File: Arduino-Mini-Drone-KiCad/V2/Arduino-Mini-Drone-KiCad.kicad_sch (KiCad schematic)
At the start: 76 parts, among them J1 NRF24, J10 BT, J11 PPM, J12 PWR, J13 Open, J2 UART, J3 Motor1, J4 Motor2, J5 Motor3, J6 Motor4, J7 CapHole, J8 MPU9250 + BMP280, J9 SPI Pads, Q1 AO3400A, Q2 AO3400A, Q3 AO3400A, Q4 AO3400A, Q5 AO3401A, SW1 Reset, SW2 Switch, U1 ATmega328P-A, U2 MIC5205YM5, U3 LP5907MFX-3.3, Y1 Crystal_GND2

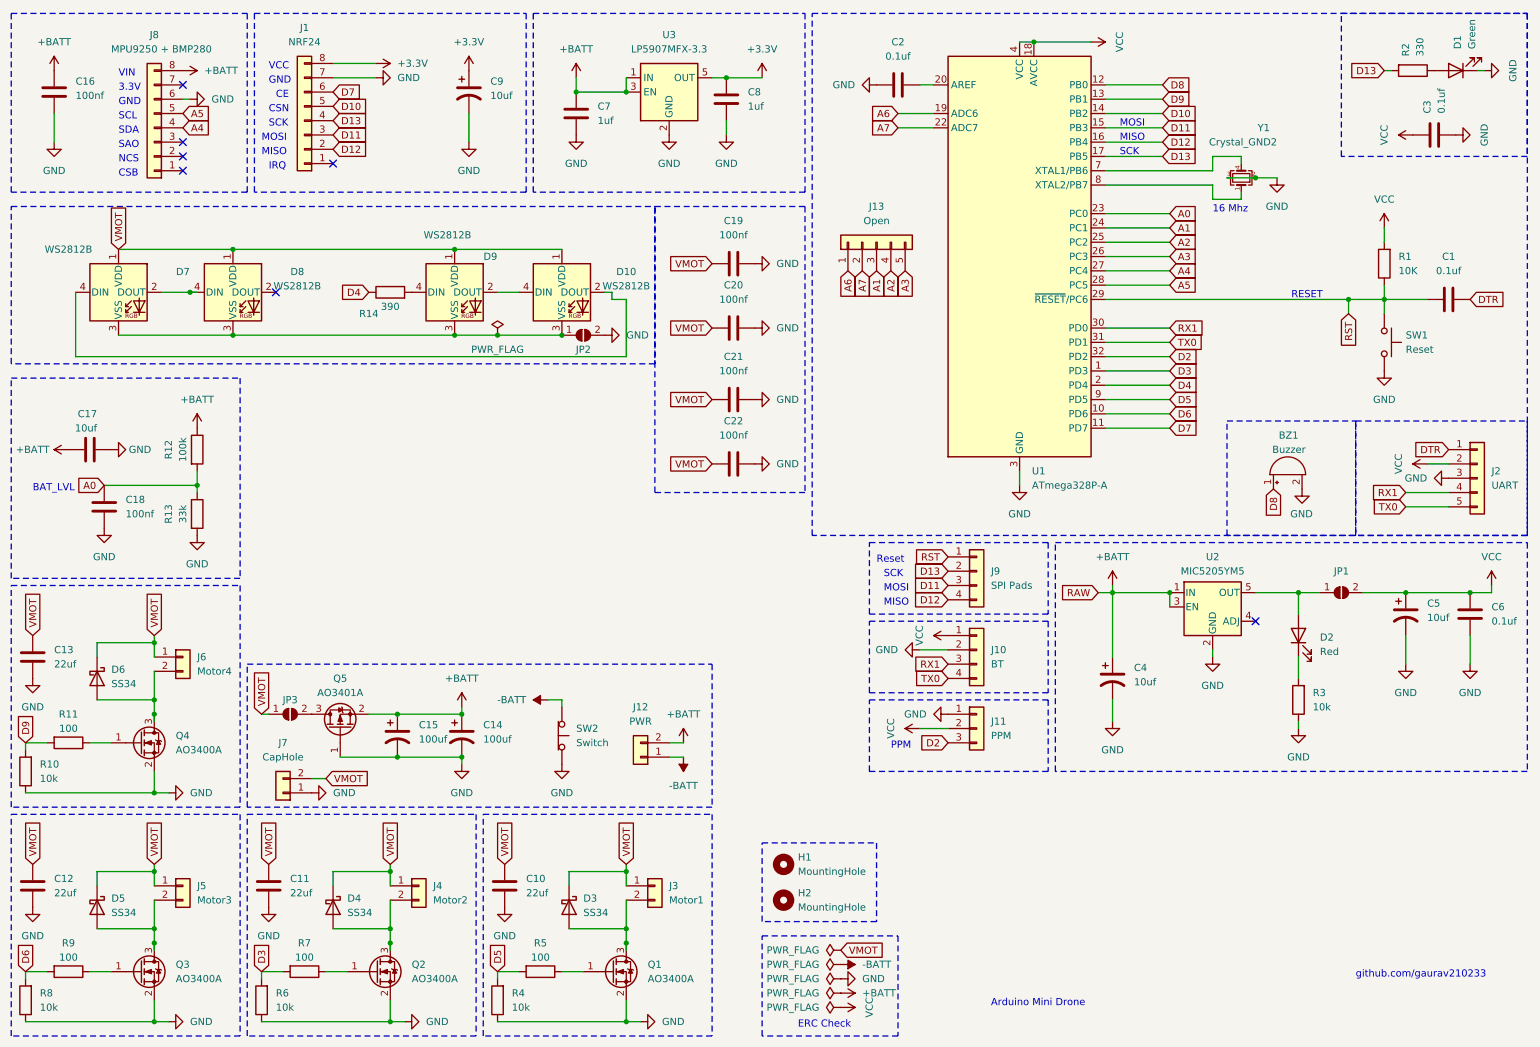
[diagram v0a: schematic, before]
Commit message: Completed Panelized PCB in V2 delete Row 2 PCB for error resolution
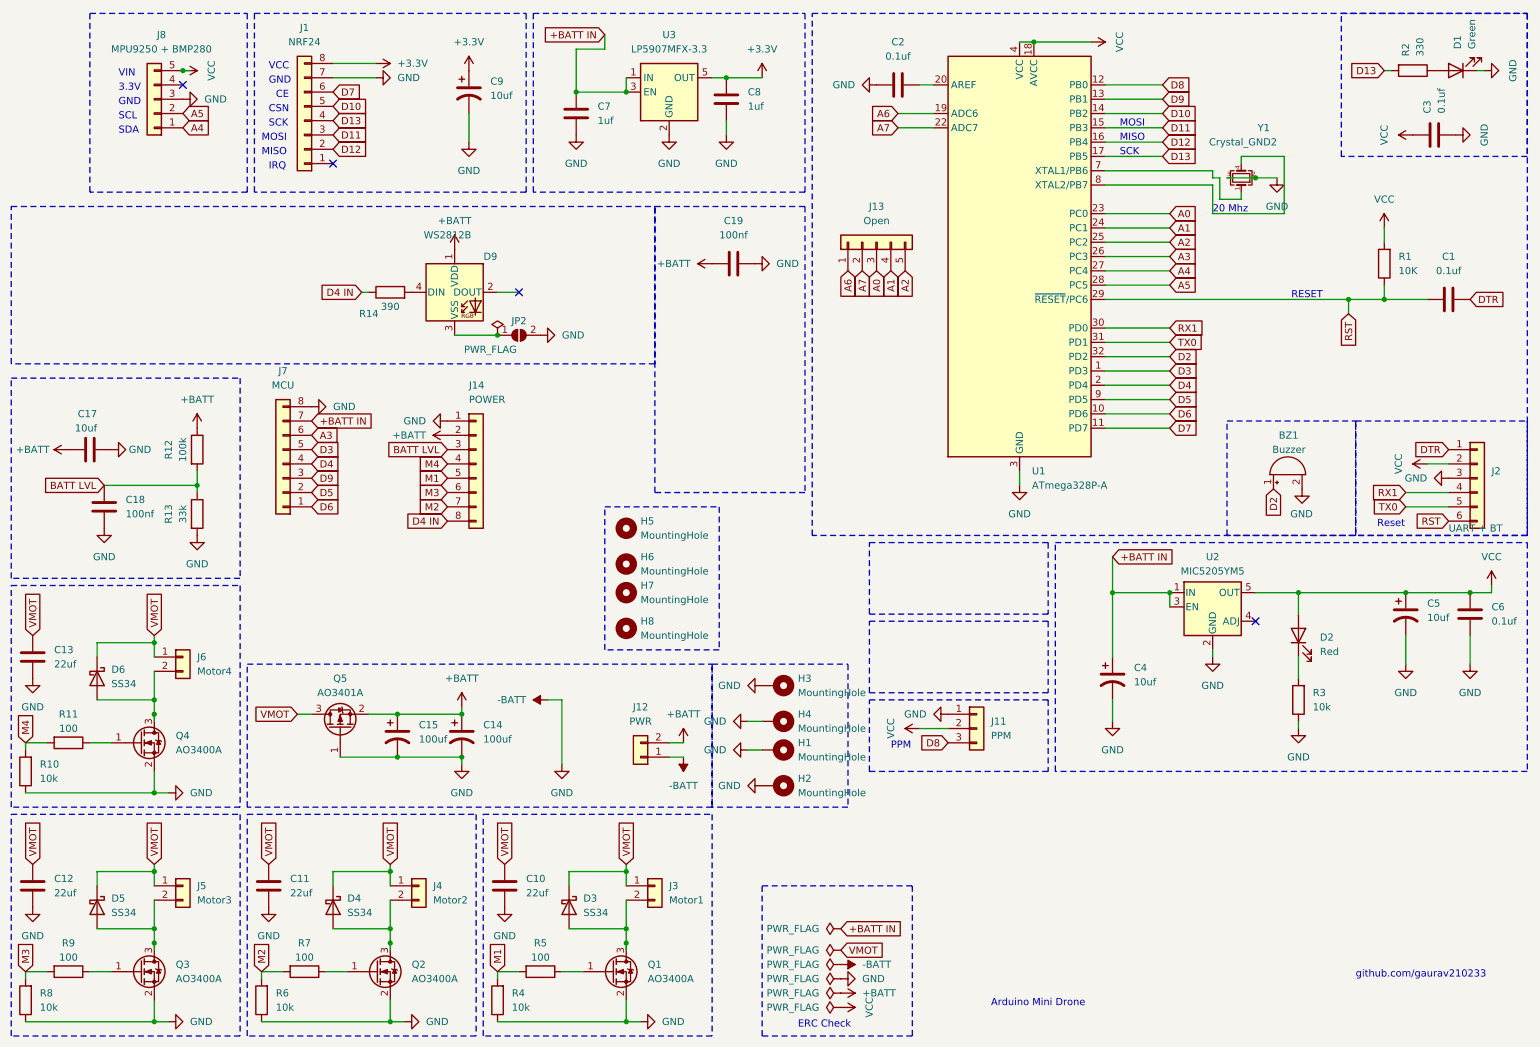
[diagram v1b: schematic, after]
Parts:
- removed C16, C20, C21, C22: 100nf, Capacitor_SMD:C_0603_1608Metric, symbol Device:C
- removed D10, D7, D8: WS2812B, LED_SMD:LED_WS2812B_PLCC4_5.0x5.0mm_P3.2mm, symbol LED:WS2812B
- removed J10: BT, Connector_PinSocket_2.54mm:PinSocket_1x04_P2.54mm_Vertical, symbol Connector_Generic:Conn_01x04
- removed J7: CapHole, Connector_PinSocket_2.54mm:PinSocket_1x02_P2.54mm_Vertical, symbol Connector_Generic:Conn_01x02
- removed J9: SPI Pads, Connector_PinHeader_2.54mm:PinHeader_1x04_P2.54mm_Vertical, symbol Connector_Generic:Conn_01x04
- removed JP1: Power isolation jumper (low power applications), Jumper:SolderJumper-2_P1.3mm_Open_Pad1.0x1.5mm, symbol Jumper:SolderJumper_2_Open
- removed JP3: Power isolation jumper (low power applications), Connector_PinHeader_2.54mm:PinHeader_1x02_P2.54mm_Vertical, symbol Jumper:SolderJumper_2_Open
- removed SW1: Reset, Button_Switch_SMD:SW_Tactile_SPST_NO_Straight_CK_PTS636Sx25SMTRLFS, symbol Switch:SW_Push
- removed SW2: Switch, Button_Switch_THT:SW_CuK_OS102011MA1QN1_SPDT_Angled, symbol Switch:SW_Push_Open
- added H3, H4: MountingHole, MountingHole:MountingHole_2.2mm_M2_Pad_Via, symbol Mechanical:MountingHole_Pad
- added H5, H6, H7, H8: MountingHole, MountingHole:MountingHole_2.2mm_M2_Pad_Via, symbol Mechanical:MountingHole
- added J14: POWER, Connector_PinHeader_1.27mm:PinHeader_1x08_P1.27mm_Vertical, symbol Connector_Generic:Conn_01x08
- added J7: MCU, Connector_PinHeader_1.27mm:PinHeader_1x08_P1.27mm_Vertical, symbol Connector_Generic:Conn_01x08
- BZ1: footprint Connector_PinHeader_2.54mm:PinHeader_1x02_P2.54mm_Vertical -> Connector_PinHeader_1.27mm:PinHeader_1x02_P1.27mm_Vertical
- C1, C2, C3, C6: footprint Capacitor_SMD:C_0402_1005Metric -> Capacitor_SMD:C_0603_1608Metric_Pad1.08x0.95mm_HandSolder
- C10, C11, C12, C13: footprint Capacitor_SMD:C_0603_1608Metric -> Capacitor_SMD:C_0805_2012Metric_Pad1.18x1.45mm_HandSolder
- C14, C15: footprint Capacitor_Tantalum_SMD:CP_EIA-6032-15_Kemet-U -> Capacitor_Tantalum_SMD:CP_EIA-3528-12_Kemet-T_Pad1.50x2.35mm_HandSolder
- C17, C18, C19, C7, C8: footprint Capacitor_SMD:C_0603_1608Metric -> Capacitor_SMD:C_0603_1608Metric_Pad1.08x0.95mm_HandSolder
- C4, C5: footprint Capacitor_Tantalum_SMD:CP_EIA-6032-15_Kemet-U -> Capacitor_Tantalum_SMD:CP_EIA-3216-10_Kemet-I_Pad1.58x1.35mm_HandSolder
- C9: footprint Capacitor_Tantalum_SMD:CP_EIA-6032-15_Kemet-U -> Capacitor_SMD:C_1206_3216Metric_Pad1.33x1.80mm_HandSolder
- D1, D2: footprint LED_SMD:LED_0603_1608Metric -> LED_SMD:LED_0603_1608Metric_Pad1.05x0.95mm_HandSolder
- D3, D4, D5, D6: footprint Diode_SMD:D_MELF -> Diode_SMD:D_MELF_Handsoldering
- H1, H2: symbol Mechanical:MountingHole -> Mechanical:MountingHole_Pad
- J11: footprint Connector_PinSocket_2.54mm:PinSocket_1x03_P2.54mm_Vertical -> Connector_PinHeader_1.27mm:PinHeader_1x03_P1.27mm_Vertical
- J13: footprint Connector_PinHeader_2.54mm:PinHeader_1x05_P2.54mm_Vertical -> Connector_PinHeader_1.27mm:PinHeader_1x05_P1.27mm_Vertical
- J2: value UART -> UART + BT; footprint Connector_PinHeader_2.54mm:PinHeader_1x05_P2.54mm_Vertical -> Connector_PinHeader_1.27mm:PinHeader_1x06_P1.27mm_Vertical; symbol Connector_Generic:Conn_01x05 -> Connector_Generic:Conn_01x06
- J3, J4, J5, J6: footprint Connector_JST:JST_PH_B2B-PH-K_1x02_P2.00mm_Vertical -> Connector_PinHeader_1.27mm:PinHeader_1x02_P1.27mm_Vertical
- J8: footprint Connector_PinSocket_2.54mm:PinSocket_1x08_P2.54mm_Vertical -> Connector_PinSocket_2.54mm:PinSocket_1x05_P2.54mm_Vertical; symbol Connector_Generic:Conn_01x08 -> Connector_Generic:Conn_01x05
- JP2: value Power isolation jumper (low power applications) -> LED ON OFF; footprint Connector_PinHeader_2.54mm:PinHeader_1x02_P2.54mm_Vertical -> Jumper:SolderJumper-2_P1.3mm_Open_Pad1.0x1.5mm
- R1, R10, R11, R12, R13, R14, R2, R3, R4, R5, R6, R7, R8, R9: footprint Resistor_SMD:R_0603_1608Metric -> Resistor_SMD:R_0603_1608Metric_Pad0.98x0.95mm_HandSolder
- U2, U3: footprint Package_TO_SOT_SMD:SOT-23-5 -> Package_TO_SOT_SMD:SOT-23-5_HandSoldering
- Y1: footprint Crystal:Crystal_SMD_3225-4Pin_3.2x2.5mm -> Crystal:Crystal_SMD_5032-4Pin_5.0x3.2mm
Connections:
- net +BATT: now also C19.2, D9.1 (VDD), J14.2 (Pin_2); no longer C4.1, C7.2, J8.8 (Pin_8), U2.1 (IN), U2.3 (EN), U3.1 (IN), U3.3 (EN)
- net -BATT: now also BZ1.2 (-), C10.1, C11.1, C12.1, C13.1, C14.2, C15.2, C17.1, C18.1, C19.1, C2.1, C3.1, C4.2, C5.2, C6.1, C7.1, C8.1, C9.2, D1.1 (K), H1.1, H2.1, J1.7 (Pin_7), J11.1 (Pin_1), J2.3 (Pin_3), J8.3 (Pin_3), JP2.2 (B), Q1.2 (S), Q2.2 (S), Q3.2 (S), Q4.2 (S), Q5.1 (G), R10.1, R13.2, R3.1, R4.1, R6.1, R8.1, U1.21 (GND), U1.3 (GND), U1.5 (GND), U2.2 (GND), U3.2 (GND), Y1.2, Y1.3, H3.1, H4.1, J14.1 (Pin_1), J7.8 (Pin_8)
- net A0: now also J13.3 (Pin_3); no longer C18.2, R12.2, R13.1
- net A1: now also J13.4 (Pin_4); no longer J13.3 (Pin_3)
- net A2: now also J13.5 (Pin_5); no longer J13.4 (Pin_4)
- net A3: now also J7.6 (Pin_6); no longer J13.5 (Pin_5)
- net A4: now also J8.1 (Pin_1); no longer J8.4 (Pin_4)
- net A5: now also J8.2 (Pin_2); no longer J8.5 (Pin_5)
- net D2: now also BZ1.1 (+); no longer J11.3 (Pin_3)
- net D3: now also J7.5 (Pin_5); no longer R6.2, R7.2
- net D4: now also J7.4 (Pin_4); no longer R14.1
- net D5: now also J7.2 (Pin_2); no longer R4.2, R5.2
- net D6: now also J7.1 (Pin_1); no longer R8.2, R9.2
- net D8: now also J11.3 (Pin_3); no longer BZ1.1 (+)
- net D9: now also J7.3 (Pin_3); no longer R10.2, R11.2
- net RST: now also J2.6 (Pin_6)
- net VCC: now also D2.2 (A), J8.5 (Pin_5), U2.5 (OUT)
- net VMOT: now also Q5.3 (D); no longer C19.2, D9.1 (VDD)
- net at U1.7 (XTAL1/PB6): now also Y1.1; no longer Y1.4
- net at U1.8 (XTAL2/PB7): now also Y1.4; no longer Y1.1
- removed net GND: BZ1.2 (-), C10.1, C11.1, C12.1, C13.1, C14.2, C15.2, C17.1, C18.1, C19.1, C2.1, C3.1, C4.2, C5.2, C6.1, C7.1, C8.1, C9.2, D1.1 (K), J1.7 (Pin_7), J11.1 (Pin_1), J2.3 (Pin_3), J8.6 (Pin_6), JP2.2 (B), Q1.2 (S), Q2.2 (S), Q3.2 (S), Q4.2 (S), Q5.1 (G), R10.1, R13.2, R3.1, R4.1, R6.1, R8.1, U1.21 (GND), U1.3 (GND), U1.5 (GND), U2.2 (GND), U3.2 (GND), Y1.2, Y1.3
- new net +BATT IN: C4.1, C7.2, J7.7 (Pin_7), U2.1 (IN), U2.3 (EN), U3.1 (IN), U3.3 (EN)
- new net BATT LVL: C18.2, J14.3 (Pin_3), R12.2, R13.1
- new net D4 IN: J14.8 (Pin_8), R14.1
- new net M1: J14.5 (Pin_5), R4.2, R5.2
- new net M2: J14.7 (Pin_7), R6.2, R7.2
- new net M3: J14.6 (Pin_6), R8.2, R9.2
- new net M4: J14.4 (Pin_4), R10.2, R11.2
- no-connect marks 7 -> 4
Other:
- note added: "20 Mhz"
- note removed: "16 Mhz"
- note removed: "BAT_LVL"
- note removed: "CSB"
- note removed: "NCS"
- note removed: "SAO"
- moved on the sheet: JP2
